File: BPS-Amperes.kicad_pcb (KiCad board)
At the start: 2 copper layers, 40 x 50 mm, 38 parts, among them J1 Conn_02x10_Odd_Even, J2 ShuntConn, J3 PassthroughConn, J4 TestConn, J5 Conn_01x02, U1 INA186A3IDDFT, U2 OPA2196, U3 LTC2315, U4 REF1930AIDDCT

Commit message: Initial Analog Circuit
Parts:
- moved C2 37.1 mm to (138.7, 103.6), turned to -90 degrees
- moved R2 36.1 mm to (136.0, 105.4), turned to 180 degrees
- moved R1 35.0 mm to (136.0, 102.8), turned to 180 degrees
- moved U1 34.2 mm to (141.5, 102.4), turned to -90 degrees
- moved C8 2.71 mm to (126.8, 115.8)
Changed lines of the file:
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@@
   )
   (footprint "Capacitor_SMD:C_0805_2012Metric" (layer "B.Cu")
-    (at 125.14 113.6626 180)
+    (at 126.764 115.8348 180)
     (descr "Capacitor SMD 0805 (2012 Metric), square (rectangular) end terminal, IPC_7351 nominal, (Body size source: IPC-SM-782 page 76, https://www.pcb-3d.com/wordpress/wp-content/uploads/ipc-sm-782a_amendment_1_and_2.pdf, https://docs.google.com/spreadsheets/d/1BsfQQcO9C6DZCsRaXUlFlo91Tg2WpOkGARC1WS5S8t0/edit?usp=sharing), generated with kicad-footprint-generator")
     (tags "capacitor")
@@
   )
   (footprint "Resistor_SMD:R_0805_2012Metric" (layer "B.Cu")
-    (at 100.9634 101.8223 90)
+    (at 135.9944 102.83 180)
     (descr "Resistor SMD 0805 (2012 Metric), square (rectangular) end terminal, IPC_7351 nominal, (Body size source: IPC-SM-782 page 72, https://www.pcb-3d.com/wordpress/wp-content/uploads/ipc-sm-782a_amendment_1_and_2.pdf), generated with kicad-footprint-generator")
     (tags "resistor")
@@
     (property "ki_keywords" "r resistor")
     (attr smd)
-    (fp_text reference "R1" (at 2.6435 0.127 90) (layer "B.SilkS")
+    (fp_text reference "R1" (at 0.0508 1.5748) (layer "B.SilkS")
         (effects (font (size 1 1) (thickness 0.15)) (justify mirror))
     )
-    (fp_text value "1.2k" (at -0.0235 1.778 90) (layer "B.Fab")
+    (fp_text value "1.2k" (at -0.0235 1.778) (layer "B.Fab")
         (effects (font (size 1 1) (thickness 0.15)) (justify mirror))
     )
-    (fp_text user "${REFERENCE}" (at 0 0 90) (layer "B.Fab")
+    (fp_text user "${REFERENCE}" (at 0 0) (layer "B.Fab")
         (effects (font (size 0.5 0.5) (thickness 0.08)) (justify mirror))
     )
@@
     (fp_line (start 1 0.625) (end 1 -0.625)
       (stroke (width 0.1) (type solid)) (layer "B.Fab"))
-    (pad "1" smd roundrect (at -0.9125 0 90) (size 1.025 1.4) (layers "B.Cu" "B.Paste" "B.Mask") (roundrect_rratio 0.243902)
+    (pad "1" smd roundrect (at -0.9125 0 180) (size 1.025 1.4) (layers "B.Cu" "B.Paste" "B.Mask") (roundrect_rratio 0.243902)
       (net 20 "/RSHH") (pintype "passive"))
-    (pad "2" smd roundrect (at 0.9125 0 90) (size 1.025 1.4) (layers "B.Cu" "B.Paste" "B.Mask") (roundrect_rratio 0.243902)
+    (pad "2" smd roundrect (at 0.9125 0 180) (size 1.025 1.4) (layers "B.Cu" "B.Paste" "B.Mask") (roundrect_rratio 0.243902)
       (net 31 "Net-(J2-Pin_2)") (pintype "passive"))
     (model "${KICAD6_3DMODEL_DIR}/Resistor_SMD.3dshapes/R_0805_2012Metric.wrl"
@@
   )
   (footprint "Resistor_SMD:R_0805_2012Metric" (layer "B.Cu")
-    (at 100.014 108.4273 -90)
+    (at 135.9944 105.37 180)
     (descr "Resistor SMD 0805 (2012 Metric), square (rectangular) end terminal, IPC_7351 nominal, (Body size source: IPC-SM-782 page 72, https://www.pcb-3d.com/wordpress/wp-content/uploads/ipc-sm-782a_amendment_1_and_2.pdf), generated with kicad-footprint-generator")
     (tags "resistor")
@@
     (property "ki_keywords" "r resistor")
     (attr smd)
-    (fp_text reference "R2" (at -2.667 0 90) (layer "B.SilkS")
+    (fp_text reference "R2" (at 0.0508 -1.6764) (layer "B.SilkS")
         (effects (font (size 1 1) (thickness 0.15)) (justify mirror))
     )
-    (fp_text value "1.2k" (at 0.127 1.651 90) (layer "B.Fab")
+    (fp_text value "1.2k" (at 0.127 1.651) (layer "B.Fab")
         (effects (font (size 1 1) (thickness 0.15)) (justify mirror))
     )
-    (fp_text user "${REFERENCE}" (at 0 0 90) (layer "B.Fab")
+    (fp_text user "${REFERENCE}" (at 0 0) (layer "B.Fab")
         (effects (font (size 0.5 0.5) (thickness 0.08)) (justify mirror))
     )
@@
     (fp_line (start 1 0.625) (end 1 -0.625)
       (stroke (width 0.1) (type solid)) (layer "B.Fab"))
-    (pad "1" smd roundrect (at -0.9125 0 270) (size 1.025 1.4) (layers "B.Cu" "B.Paste" "B.Mask") (roundrect_rratio 0.243902)
+    (pad "1" smd roundrect (at -0.9125 0 180) (size 1.025 1.4) (layers "B.Cu" "B.Paste" "B.Mask") (roundrect_rratio 0.243902)
       (net 21 "/RSHL") (pintype "passive"))
-    (pad "2" smd roundrect (at 0.9125 0 270) (size 1.025 1.4) (layers "B.Cu" "B.Paste" "B.Mask") (roundrect_rratio 0.243902)
+    (pad "2" smd roundrect (at 0.9125 0 180) (size 1.025 1.4) (layers "B.Cu" "B.Paste" "B.Mask") (roundrect_rratio 0.243902)
       (net 4 "GND") (pintype "passive"))
     (model "${KICAD6_3DMODEL_DIR}/Resistor_SMD.3dshapes/R_0805_2012Metric.wrl"
@@
   )
   (footprint "Package_TO_SOT_SMD:SOT-23-8" (layer "B.Cu")
-    (at 107.5729 98.3308 180)
+    (at 141.5414 102.3927 -90)
     (descr "SOT, 8 Pin (https://www.jedec.org/sites/default/files/docs/Mo-178c.PDF variant BA), generated with kicad-footprint-generator ipc_gullwing_generator.py")
     (tags "SOT TO_SOT_SMD")
@@
     (property "Sheetname" "")
     (attr smd)
-    (fp_text reference "U1" (at 0 2.4) (layer "B.SilkS")
+    (fp_text reference "U1" (at -2.8139 0.0606 -180) (layer "B.SilkS")
         (effects (font (size 1 1) (thickness 0.15)) (justify mirror))
     )
-    (fp_text value "INA186A3IDDFT " (at -4.318 -3.175 90) (layer "B.Fab")
+    (fp_text value "INA186A3IDDFT " (at -0.4263 -2.5302 90) (layer "B.Fab")
         (effects (font (size 1 1) (thickness 0.15)) (justify mirror))
     )
-    (fp_text user "${REFERENCE}" (at 0 0) (layer "B.Fab")
+    (fp_text user "${REFERENCE}" (at 0 0 90) (layer "B.Fab")
         (effects (font (size 0.4 0.4) (thickness 0.06)) (justify mirror))
     )
@@
     (fp_line (start 0.8 1.45) (end 0.8 -1.45)
       (stroke (width 0.1) (type solid)) (layer "B.Fab"))
-    (pad "1" smd roundrect (at -1.1375 0.975 180) (size 1.325 0.5) (layers "B.Cu" "B.Paste" "B.Mask") (roundrect_rratio 0.25)
+    (pad "1" smd roundrect (at -1.1375 0.975 270) (size 1.325 0.5) (layers "B.Cu" "B.Paste" "B.Mask") (roundrect_rratio 0.25)
       (net 19 "+3V0") (pinfunction "VS") (pintype "power_in"))
-    (pad "2" smd roundrect (at -1.1375 0.325 180) (size 1.325 0.5) (layers "B.Cu" "B.Paste" "B.Mask") (roundrect_rratio 0.25)
+    (pad "2" smd roundrect (at -1.1375 0.325 270) (size 1.325 0.5) (layers "B.Cu" "B.Paste" "B.Mask") (roundrect_rratio 0.25)
       (net 19 "+3V0") (pinfunction "EN") (pintype "input"))
-    (pad "3" smd roundrect (at -1.1375 -0.325 180) (size 1.325 0.5) (layers "B.Cu" "B.Paste" "B.Mask") (roundrect_rratio 0.25)
+    (pad "3" smd roundrect (at -1.1375 -0.325 270) (size 1.325 0.5) (layers "B.Cu" "B.Paste" "B.Mask") (roundrect_rratio 0.25)
       (net 26 "+1V5") (pinfunction "REF") (pintype "input"))
-    (pad "4" smd roundrect (at -1.1375 -0.975 180) (size 1.325 0.5) (layers "B.Cu" "B.Paste" "B.Mask") (roundrect_rratio 0.25)
+    (pad "4" smd roundrect (at -1.1375 -0.975 270) (size 1.325 0.5) (layers "B.Cu" "B.Paste" "B.Mask") (roundrect_rratio 0.25)
       (net 4 "GND") (pinfunction "GND") (pintype "power_in"))
-    (pad "5" smd roundrect (at 1.1375 -0.975 180) (size 1.325 0.5) (layers "B.Cu" "B.Paste" "B.Mask") (roundrect_rratio 0.25)
+    (pad "5" smd roundrect (at 1.1375 -0.975 270) (size 1.325 0.5) (layers "B.Cu" "B.Paste" "B.Mask") (roundrect_rratio 0.25)
       (net 32 "Net-(U1-OUT)") (pinfunction "OUT") (pintype "output"))
-    (pad "6" smd roundrect (at 1.1375 -0.325 180) (size 1.325 0.5) (layers "B.Cu" "B.Paste" "B.Mask") (roundrect_rratio 0.25)
+    (pad "6" smd roundrect (at 1.1375 -0.325 270) (size 1.325 0.5) (layers "B.Cu" "B.Paste" "B.Mask") (roundrect_rratio 0.25)
       (net 35 "unconnected-(U1-NC-Pad6)") (pinfunction "NC") (pintype "no_connect"))
-    (pad "7" smd roundrect (at 1.1375 0.325 180) (size 1.325 0.5) (layers "B.Cu" "B.Paste" "B.Mask") (roundrect_rratio 0.25)
+    (pad "7" smd roundrect (at 1.1375 0.325 270) (size 1.325 0.5) (layers "B.Cu" "B.Paste" "B.Mask") (roundrect_rratio 0.25)
       (net 20 "/RSHH") (pinfunction "IN+") (pintype "input"))
-    (pad "8" smd roundrect (at 1.1375 0.975 180) (size 1.325 0.5) (layers "B.Cu" "B.Paste" "B.Mask") (roundrect_rratio 0.25)
+    (pad "8" smd roundrect (at 1.1375 0.975 270) (size 1.325 0.5) (layers "B.Cu" "B.Paste" "B.Mask") (roundrect_rratio 0.25)
       (net 21 "/RSHL") (pinfunction "IN-") (pintype "input"))
     (model "${KICAD6_3DMODEL_DIR}/Package_TO_SOT_SMD.3dshapes/SOT-23-8.wrl"
@@
   )
   (footprint "Capacitor_SMD:C_0805_2012Metric" (layer "B.Cu")
-    (at 102.314 96.4648 90)
+    (at 138.7376 103.592 -90)
     (descr "Capacitor SMD 0805 (2012 Metric), square (rectangular) end terminal, IPC_7351 nominal, (Body size source: IPC-SM-782 page 76, https://www.pcb-3d.com/wordpress/wp-content/uploads/ipc-sm-782a_amendment_1_and_2.pdf, https://docs.google.com/spreadsheets/d/1BsfQQcO9C6DZCsRaXUlFlo91Tg2WpOkGARC1WS5S8t0/edit?usp=sharing), generated with kicad-footprint-generator")
     (tags "capacitor")
@@
     (property "ki_keywords" "capacitor cap")
     (attr smd)
-    (fp_text reference "C2" (at -2.86 0 90) (layer "B.SilkS")
+    (fp_text reference "C2" (at -2.86 0) (layer "B.SilkS")
         (effects (font (size 1 1) (thickness 0.15)) (justify mirror))
     )
@@
     (fp_line (start 1 0.625) (end 1 -0.625)
       (stroke (width 0.1) (type solid)) (layer "B.Fab"))
-    (pad "1" smd roundrect (at -0.95 0 90) (size 1 1.45) (layers "B.Cu" "B.Paste" "B.Mask") (roundrect_rratio 0.25)
+    (pad "1" smd roundrect (at -0.95 0 270) (size 1 1.45) (layers "B.Cu" "B.Paste" "B.Mask") (roundrect_rratio 0.25)
       (net 20 "/RSHH") (pintype "passive"))
-    (pad "2" smd roundrect (at 0.95 0 90) (size 1 1.45) (layers "B.Cu" "B.Paste" "B.Mask") (roundrect_rratio 0.25)
+    (pad "2" smd roundrect (at 0.95 0 270) (size 1 1.45) (layers "B.Cu" "B.Paste" "B.Mask") (roundrect_rratio 0.25)
       (net 21 "/RSHL") (pintype "passive"))
     (model "${KICAD6_3DMODEL_DIR}/Capacitor_SMD.3dshapes/C_0805_2012Metric.wrl"

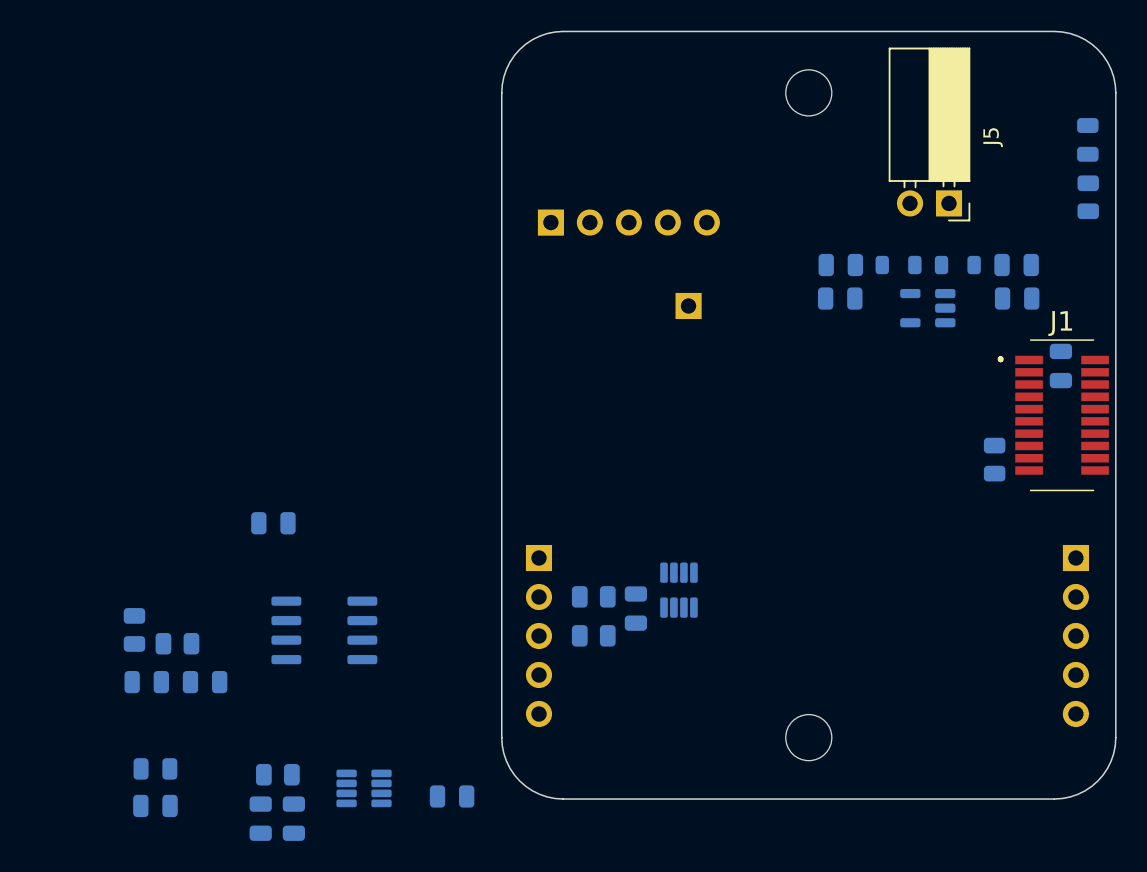
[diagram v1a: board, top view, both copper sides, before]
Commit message: put analog smd items on top and layout stuffs
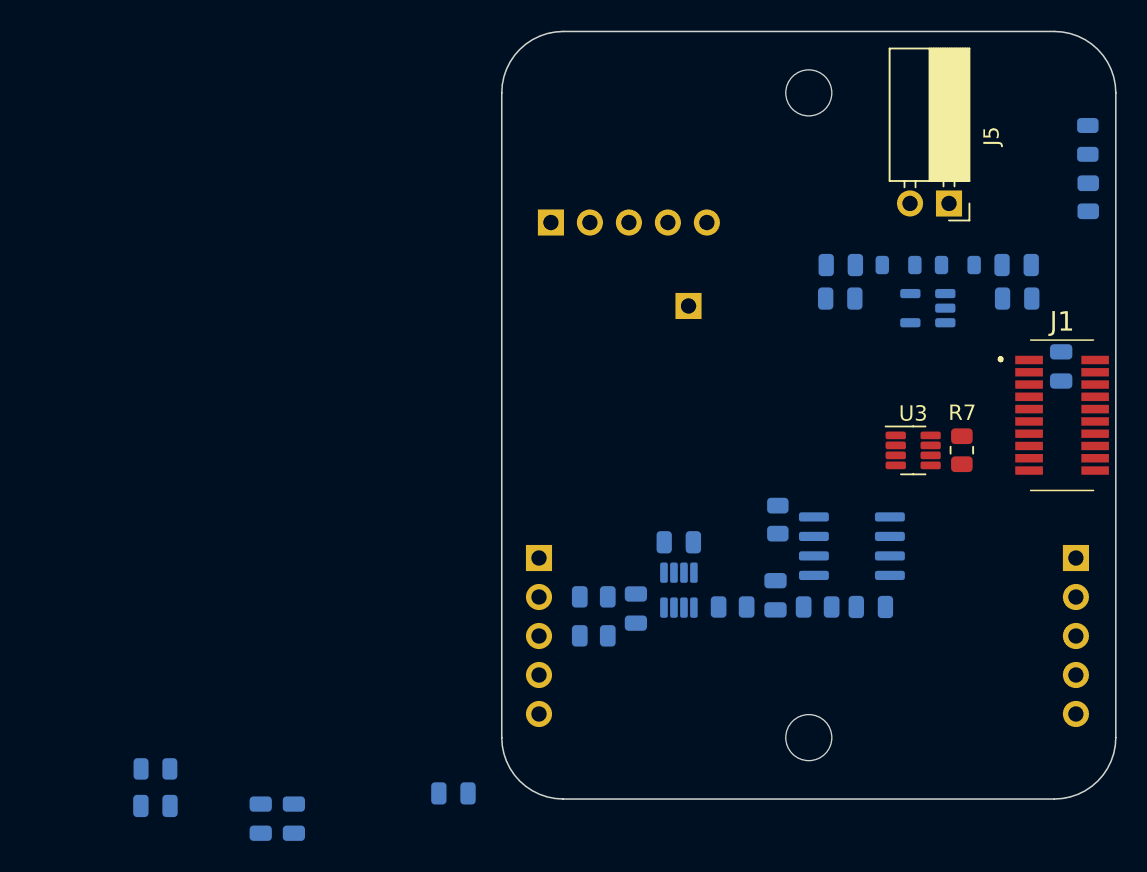
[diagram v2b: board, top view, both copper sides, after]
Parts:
- R7, U3: moved to F.Cu
- moved C4 43.6 mm to (154.0, 103.5), turned to 0 degrees
- moved U3 42.0 mm to (156.8, 93.3)
- moved R4 41.8 mm to (150.6, 103.5), turned to 0 degrees
- moved C3 41.3 mm to (147.8, 102.7), turned to 90 degrees
- moved R3 39.0 mm to (145.0, 103.5), turned to 180 degrees
- moved R5 36.6 mm to (148.0, 97.8), turned to 90 degrees
- moved U2 34.8 mm to (152.8, 99.5)
- moved C1 26.4 mm to (141.5, 99.3)
- moved R7 2.22 mm to (160.0, 93.3)
- moved C8 0.22 mm to (126.9, 115.6)

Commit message: Finished general placement of remaining components
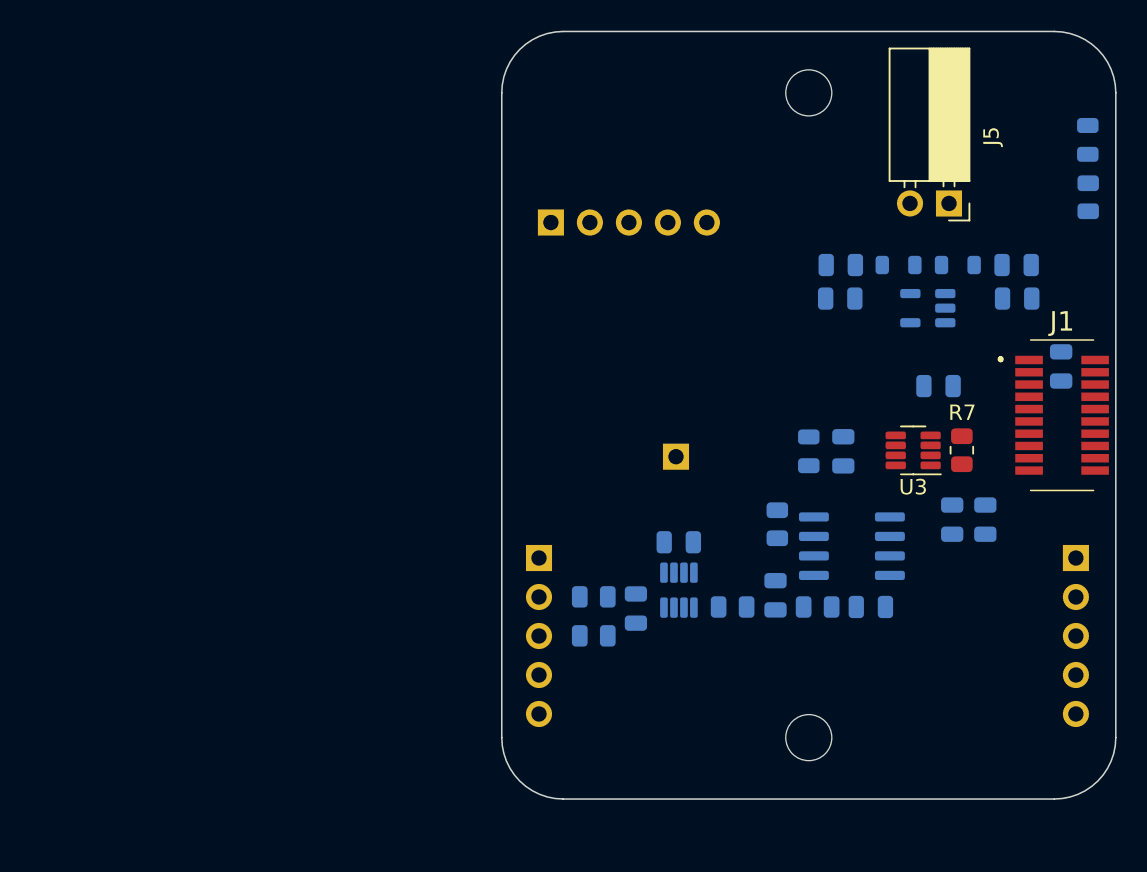
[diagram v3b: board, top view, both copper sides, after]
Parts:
- moved C5 51.1 mm to (161.5, 97.8), turned to -90 degrees
- moved C6 50.4 mm to (152.2, 93.3), turned to 90 degrees
- moved D1 47.3 mm to (150.0, 93.3), turned to 90 degrees
- moved C7 47.1 mm to (159.3, 97.8), turned to -90 degrees
- moved C8 41.3 mm to (158.4, 89.1)
- moved TP1 9.85 mm to (141.3, 93.7)
- moved R5 0.30 mm to (147.9, 98.1)
- turned U3 to 180 degrees

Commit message: fix broken layout
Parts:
- removed C8: 2.2uF, Capacitor_SMD:C_0805_2012Metric
- removed R7: 49.9, Resistor_SMD:R_0805_2012Metric
- removed U3: LTC2315, Package_TO_SOT_SMD:SOT-23-8
- D1: value 3.0V±0.05 -> 3.3V±0.05
- J5: moved to B.Cu
- moved J4 48.8 mm to (166.5, 114.1), turned to 90 degrees
- moved J5 19.6 mm to (139.7, 80.0), turned to 0 degrees
- moved C13 8.78 mm to (157.7, 86.9), turned to 0 degrees
- moved TP1 1.72 mm to (139.9, 92.7)
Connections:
- C6 pad 1: Net-(D1-K) -> /Aout
- D1 pad 1: Net-(D1-K) -> /Aout
- J1 pad 20: GNDPWR -> /Aout
- R5 pad 2: Net-(D1-K) -> /Aout
- TP1 pad 1: Net-(D1-K) -> /Aout

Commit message: Fixing spacing and reiterating on v1
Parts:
- C1, C2, C3, C4, C5, C6, C7, D1, R1, R2, R3, R4, R5, U1, U2: moved to F.Cu
- moved J4 41.9 mm to (160.2, 72.7), turned to 180 degrees
- moved D2 38.3 mm to (132.0, 85.7), turned to 0 degrees
- moved R6 33.7 mm to (135.7, 85.7), turned to 180 degrees
- moved D1 9.82 mm to (159.8, 94.5)
- moved C9 7.82 mm to (155.8, 83.3)
- moved C10 7.80 mm to (155.8, 80.8)
- moved FB2 7.48 mm to (148.9, 78.3)
- moved R5 7.45 mm to (154.0, 93.8), turned to 0 degrees
- moved FB1 6.93 mm to (153.4, 78.3)
- moved U4 6.84 mm to (151.1, 82.3)
- moved C13 6.67 mm to (151.2, 85.4)
- moved C11 5.35 mm to (146.8, 80.8)
- moved C12 5.30 mm to (146.8, 83.3)
- moved C6 5.13 mm to (157.2, 94.5)
- moved U2 3.64 mm to (149.5, 98.0), turned to 0 degrees
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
